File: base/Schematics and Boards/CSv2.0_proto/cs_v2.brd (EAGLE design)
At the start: 38.1 x 44.5 mm, 80 parts, among them J101 J-JTAG-CORTEX-NEEDLE6-LEGS, J301 HIROSE-DF40_44-PIN_CONNECTORS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, J302 HIROSE-DF40_30-PIN_CONNECTORS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, Q201 FK3303010L, Q202 DMG3415UFY4Q-7, Q203 FK3303010L, Q204 FK3303010L, U101 ATSAMD51, U102 AT25SF641-MHB-T, U201 COULOMB-MAX17262, U202 MAX77827BEWC+T, U203 SENSOR-SI7006, U204 LOADSWITCH-MIC94164, U205 LOADSWITCH-MIC94164, Y101 16M, Y102 ABS07-32.768KHZ-9-T

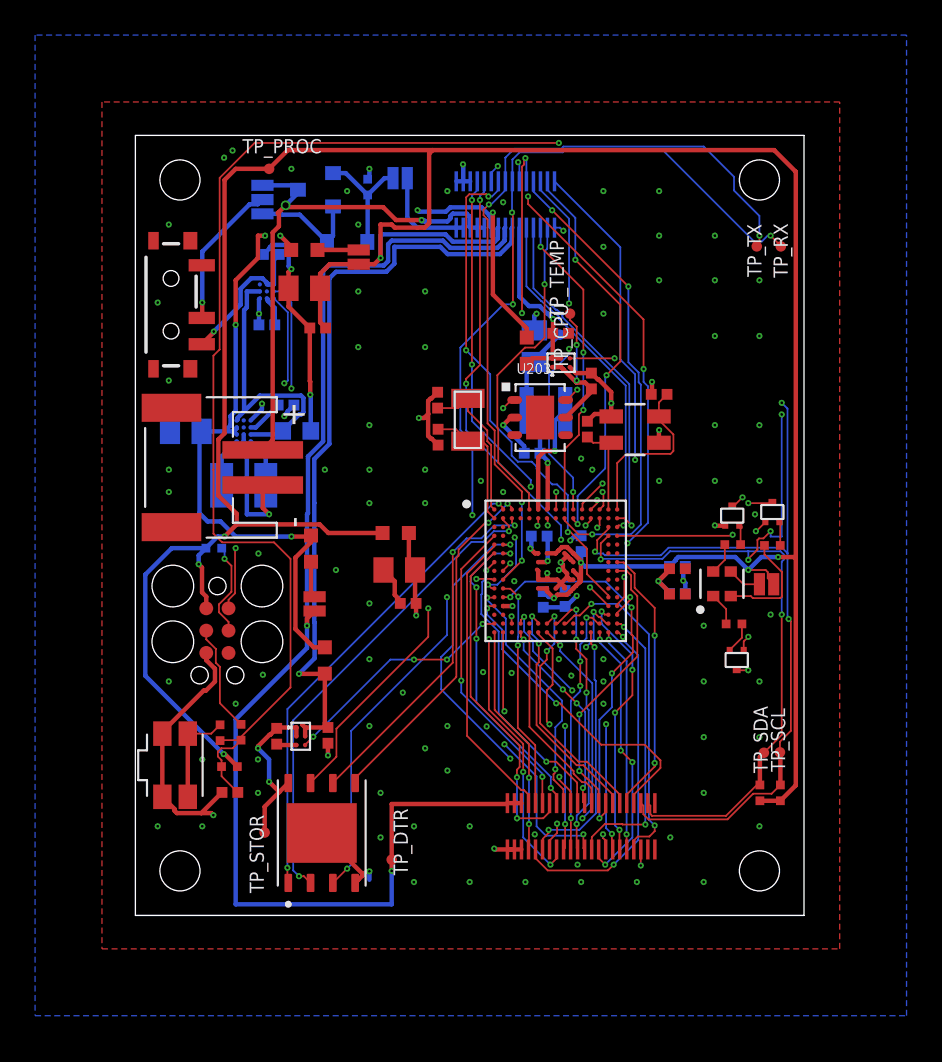
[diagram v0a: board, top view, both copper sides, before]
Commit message: All remaining DRC errors resolved
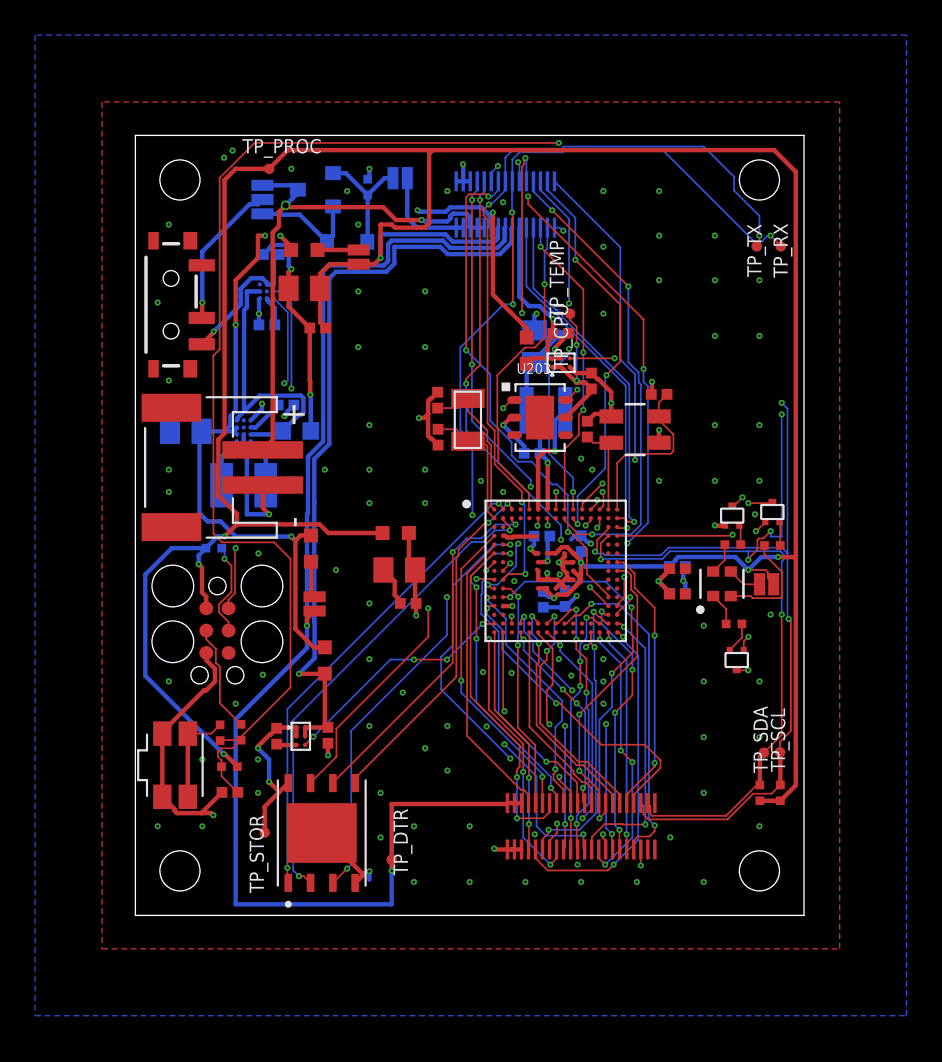
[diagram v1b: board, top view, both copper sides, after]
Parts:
- moved C105 0.15 mm to (23.2, 21.6)
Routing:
- net GND: track 82.6 -> 86.8 mm, vias 115 -> 116
- net DBG_SWDIO: track 69.0 -> 66.7 mm
- net +3V3: track 58.3 -> 57.4 mm
- net DBG_SERIAL_TX: track 44.6 -> 45.4 mm

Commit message: Fix a few items based on 1st round DFM checks with 7pcb
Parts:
- renumbered TP_CPU to CPU, TP_DTR to DTR, TP_PROC to PROC, TP_RX to RXDBG, TP_SCL to SCL, TP_SDA to SDA, TP_STOR to STOR, TP_TEMP to TEMP, TP_TX to TXDBG

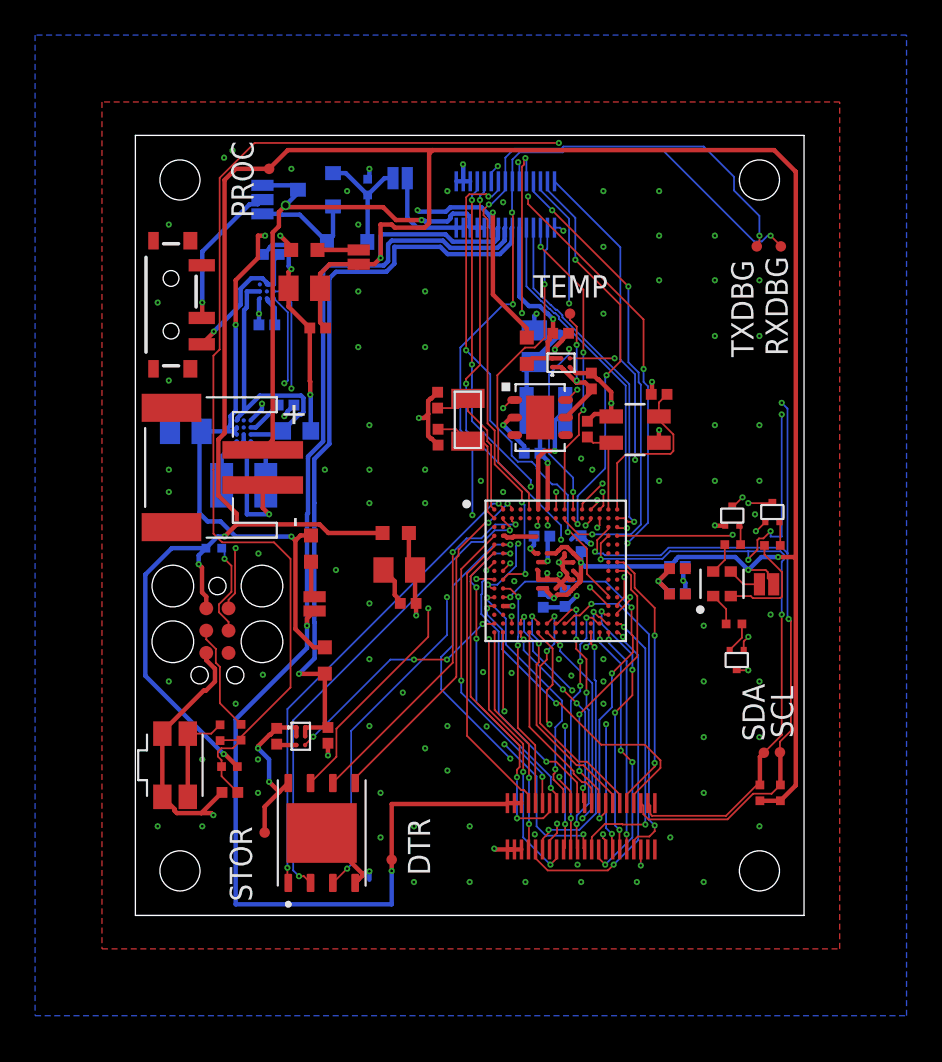
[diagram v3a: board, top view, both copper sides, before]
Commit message: Adding item outlines to Eagle as part of DFM issues
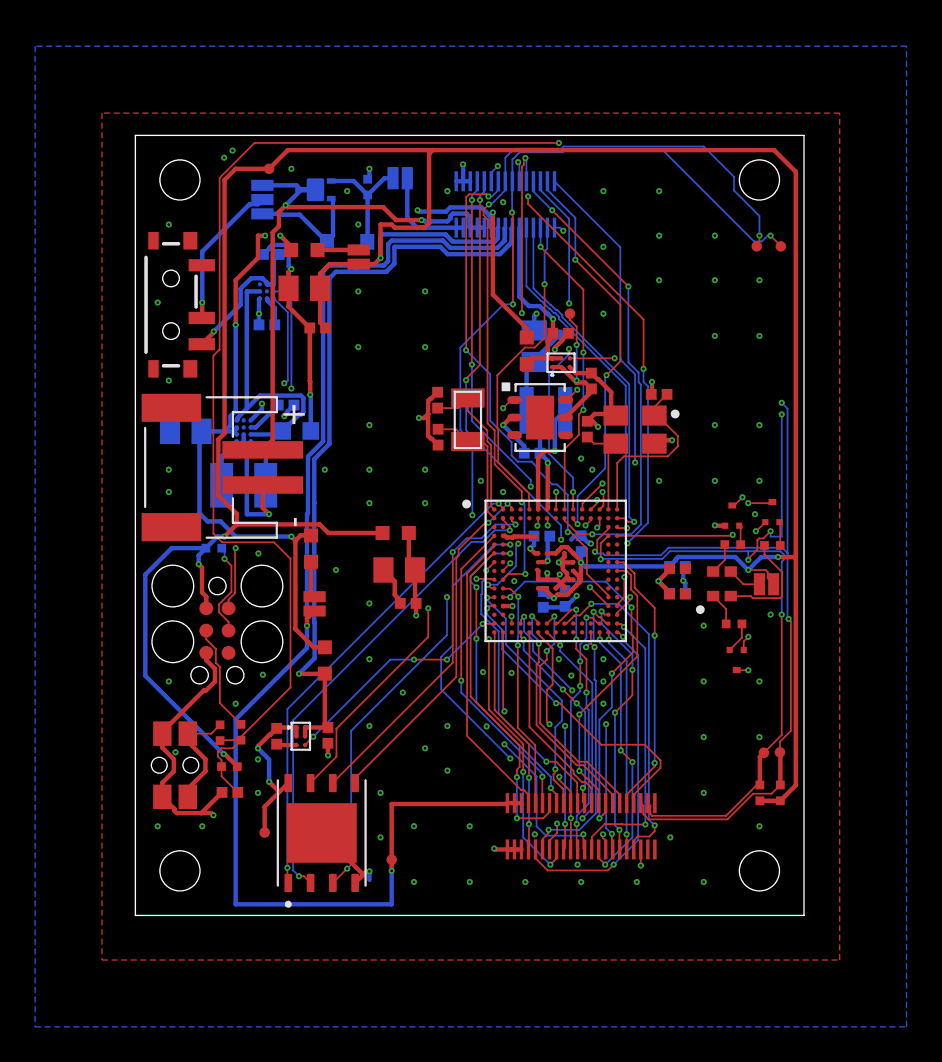
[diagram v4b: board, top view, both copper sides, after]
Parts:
- Q202: value DMG3415UFY4Q-7 -> DMG3415UFY4Q-7F; device Switches:SOT23-3 -> Switches:X2-DFN2015-3
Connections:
- net +3V7_BATT: now also Q202.3-1, Q202.3-2; no longer Q202.3
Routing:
- net GND: track 86.8 -> 88.2 mm
- net +3V7_BATT: track 30.4 -> 31.5 mm
- net N$5: track 5.65 -> 6.48 mm
- net XIN: track 9.89 -> 10.4 mm
